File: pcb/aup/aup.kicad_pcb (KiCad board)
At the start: 6 copper layers, 50 x 50 mm, 7 parts, among them IC1 MT41K128M16JT-125_K, J1 DF40C-100DS-0.4V_51, J2 DF40C-100DS-0.4V_51, J3 DF40C-100DS-0.4V_51, J4 DF40C-100DS-0.4V_51, U1 XC7A50T-FGG484, U2 FT2232HL

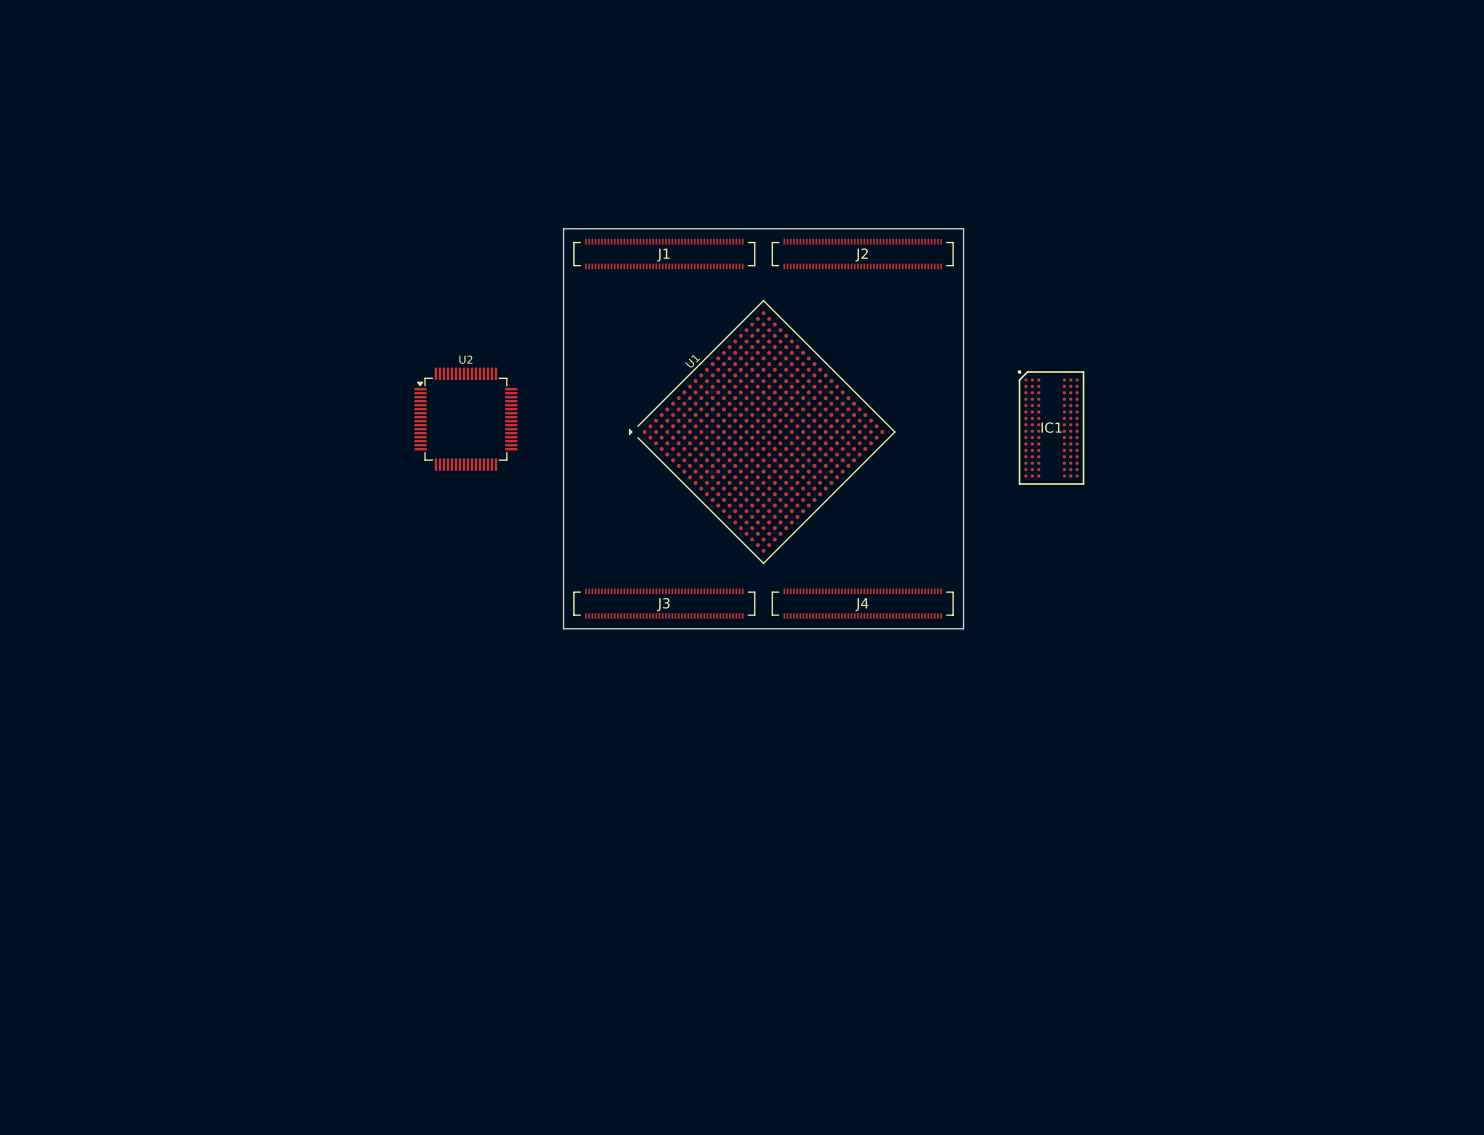
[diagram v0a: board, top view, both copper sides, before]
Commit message: Added symbols for the major components
It should be possible to do a first pass placement of ICs on the pcb as
a rough fit check.

Most imported footprints are still missing models.
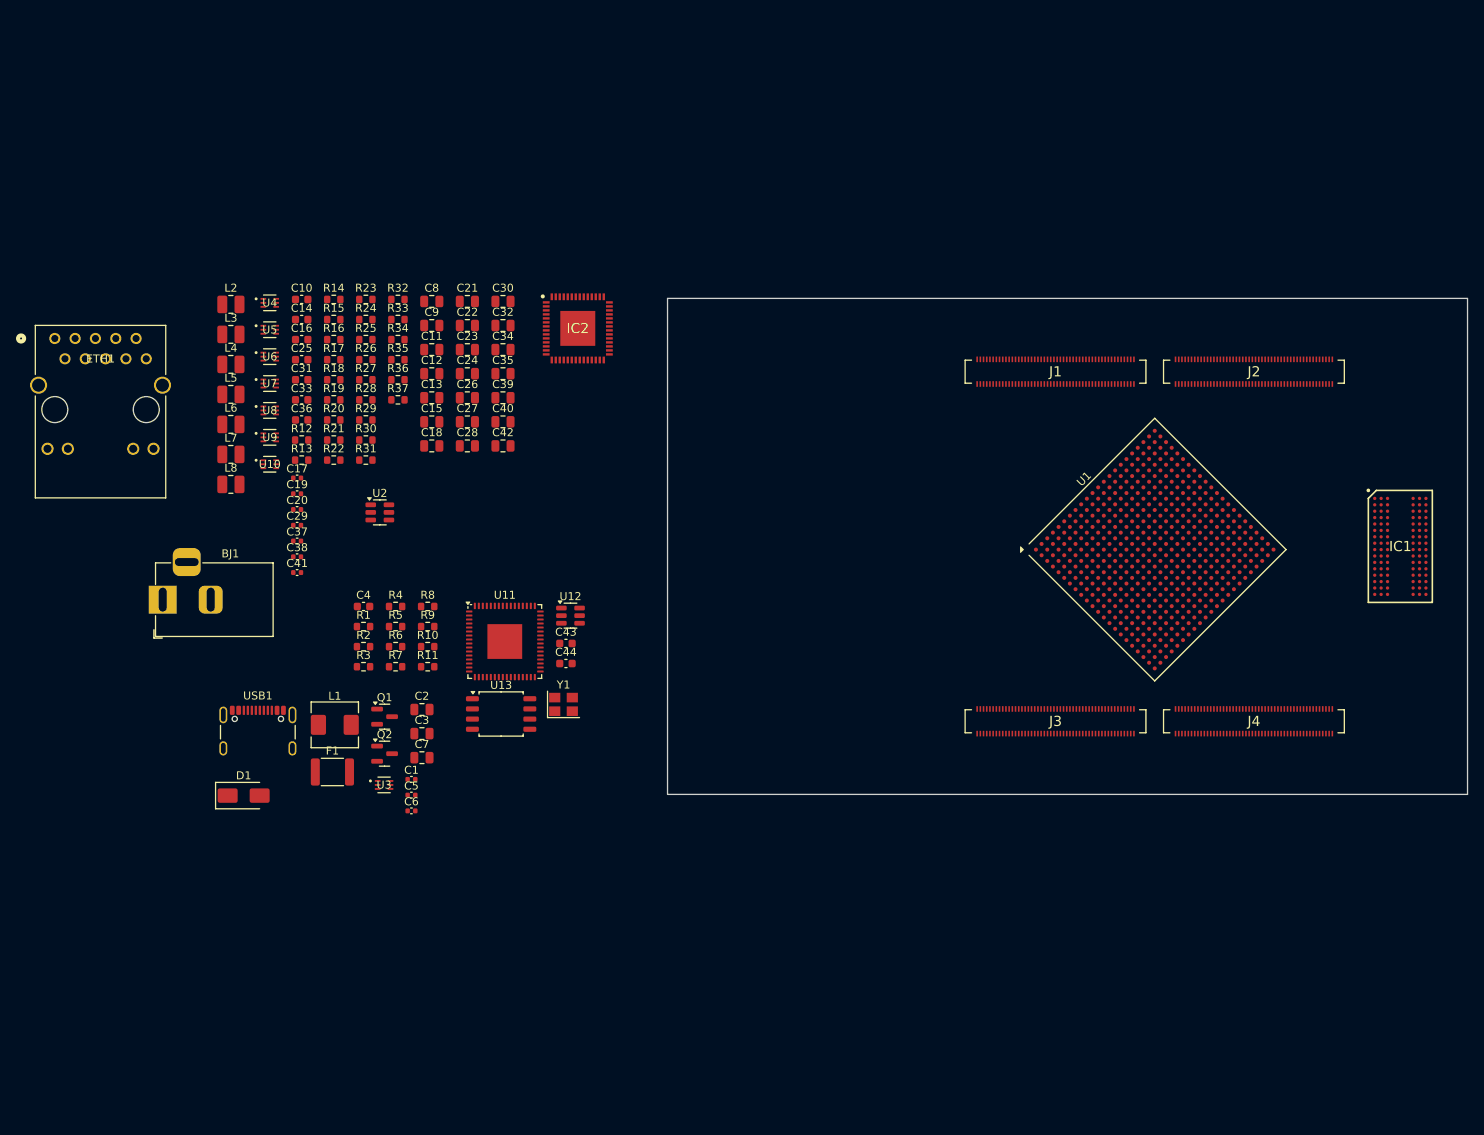
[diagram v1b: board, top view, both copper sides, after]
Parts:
- added BJ1: Barral_Jack_12V, Connector_BarrelJack:BarrelJack_Horizontal, F.Cu at (36.9, 87.4)
- added C1: 0.1uf, Capacitor_SMD:C_0402_1005Metric, F.Cu at (68.0, 109.8)
- added C10: 0.1uf/50v, Capacitor_SMD:C_0603_1608Metric, F.Cu at (54.3, 49.8)
- added C11: 10uf/50V, Capacitor_SMD:C_0805_2012Metric, F.Cu at (70.5, 56.1)
- added C12: 10uf/50V, Capacitor_SMD:C_0805_2012Metric, F.Cu at (70.5, 59.1)
- added C13: 10uf/50V, Capacitor_SMD:C_0805_2012Metric, F.Cu at (70.5, 62.1)
- added C14: 0.1uf/50v, Capacitor_SMD:C_0603_1608Metric, F.Cu at (54.3, 52.3)
- added C15: 10uf/50V, Capacitor_SMD:C_0805_2012Metric, F.Cu at (70.5, 65.1)
- added C16: 0.1uf/50v, Capacitor_SMD:C_0603_1608Metric, F.Cu at (54.3, 54.9)
- added C17: 0.1uf, Capacitor_SMD:C_0402_1005Metric, F.Cu at (53.7, 72.2)
- added C18: 22uf/25V, Capacitor_SMD:C_0805_2012Metric, F.Cu at (70.5, 68.1)
- added C19: 0.1uf, Capacitor_SMD:C_0402_1005Metric, F.Cu at (53.7, 74.1)
- added C2: 10uf/50V, Capacitor_SMD:C_0805_2012Metric, F.Cu at (69.3, 101.1)
- added C20: 0.1uf, Capacitor_SMD:C_0402_1005Metric, F.Cu at (53.7, 76.1)
- added C21: 10uf/50V, Capacitor_SMD:C_0805_2012Metric, F.Cu at (75.0, 50.1)
- added C22: 10uf/50V, Capacitor_SMD:C_0805_2012Metric, F.Cu at (75.0, 53.1)
- added C23: 22uf/25V, Capacitor_SMD:C_0805_2012Metric, F.Cu at (75.0, 56.1)
- added C24: 22uf/25V, Capacitor_SMD:C_0805_2012Metric, F.Cu at (75.0, 59.1)
- added C25: 0.1uf/50v, Capacitor_SMD:C_0603_1608Metric, F.Cu at (54.3, 57.4)
- added C26: 10uf/50V, Capacitor_SMD:C_0805_2012Metric, F.Cu at (75.0, 62.1)
- added C27: 10uf/50V, Capacitor_SMD:C_0805_2012Metric, F.Cu at (75.0, 65.1)
- added C28: 10uf/50V, Capacitor_SMD:C_0805_2012Metric, F.Cu at (75.0, 68.1)
- added C29: 0.1uf, Capacitor_SMD:C_0402_1005Metric, F.Cu at (53.7, 78.1)
- added C3: 10uf/50V, Capacitor_SMD:C_0805_2012Metric, F.Cu at (69.3, 104.1)
- added C30: 10uf/50V, Capacitor_SMD:C_0805_2012Metric, F.Cu at (79.4, 50.1)
- added C31: 0.1uf/50v, Capacitor_SMD:C_0603_1608Metric, F.Cu at (54.3, 59.9)
- added C32: 22uf/25V, Capacitor_SMD:C_0805_2012Metric, F.Cu at (79.4, 53.1)
- added C33: 0.1uf/50v, Capacitor_SMD:C_0603_1608Metric, F.Cu at (54.3, 62.4)
- added C34: 10uf/50V, Capacitor_SMD:C_0805_2012Metric, F.Cu at (79.4, 56.1)
- added C35: 10uf/50V, Capacitor_SMD:C_0805_2012Metric, F.Cu at (79.4, 59.1)
- added C36: 0.1uf/50v, Capacitor_SMD:C_0603_1608Metric, F.Cu at (54.3, 64.9)
- added C37: 0.1uf, Capacitor_SMD:C_0402_1005Metric, F.Cu at (53.7, 80.0)
- added C38: 0.1uf, Capacitor_SMD:C_0402_1005Metric, F.Cu at (53.7, 82.0)
- added C39: 22uf/25V, Capacitor_SMD:C_0805_2012Metric, F.Cu at (79.4, 62.1)
- added C4: 0.1uf/50v, Capacitor_SMD:C_0603_1608Metric, F.Cu at (62.0, 88.2)
- added C40: 22uf/25V, Capacitor_SMD:C_0805_2012Metric, F.Cu at (79.4, 65.1)
- added C41: 0.1uf, Capacitor_SMD:C_0402_1005Metric, F.Cu at (53.7, 84.0)
- added C42: 22uf/25V, Capacitor_SMD:C_0805_2012Metric, F.Cu at (79.4, 68.1)
- added C43: 30pf, Capacitor_SMD:C_0603_1608Metric, F.Cu at (87.3, 92.8)
- added C44: 30pf, Capacitor_SMD:C_0603_1608Metric, F.Cu at (87.3, 95.3)
- added C5: 33pf, Capacitor_SMD:C_0402_1005Metric, F.Cu at (68.0, 111.8)
- added C6: 0.1uf, Capacitor_SMD:C_0402_1005Metric, F.Cu at (68.0, 113.8)
- added C7: 22uf/25V, Capacitor_SMD:C_0805_2012Metric, F.Cu at (69.3, 107.1)
- added C8: 10uf/50V, Capacitor_SMD:C_0805_2012Metric, F.Cu at (70.5, 50.1)
- added C9: 10uf/50V, Capacitor_SMD:C_0805_2012Metric, F.Cu at (70.5, 53.1)
- added D1: SS34, Diode_SMD:D_SMA, F.Cu at (47.0, 111.8)
- added ETH1: HR911130A, !Misc:HR911130A_HAN, F.Cu at (23.4, 54.7)
- added F1: 2A, Fuse:Fuse_1812_4532Metric, F.Cu at (58.1, 108.9)
- added IC2: 88E1512-A0-NNP2C000, !Misc:QFN50P800X800X100-57N-D, F.Cu at (88.8, 53.5)
- added L1: 2.2uH/5A, Inductor_SMD:L_Sunlord_MWSA0518S, F.Cu at (58.4, 103.0)
- added L2: 1uH/2A, Inductor_SMD:L_1008_2520Metric, F.Cu at (45.4, 50.5)
- added L3: 1uH/2A, Inductor_SMD:L_1008_2520Metric, F.Cu at (45.4, 54.2)
- added L4: 2.2uH/2A, Inductor_SMD:L_1008_2520Metric, F.Cu at (45.4, 58.0)
- added L5: 1uH/2A, Inductor_SMD:L_1008_2520Metric, F.Cu at (45.4, 61.7)
- added L6: 2.2uH/2A, Inductor_SMD:L_1008_2520Metric, F.Cu at (45.4, 65.5)
- added L7: 2.2uH/2A, Inductor_SMD:L_1008_2520Metric, F.Cu at (45.4, 69.2)
- added L8: 1uH/2A, Inductor_SMD:L_1008_2520Metric, F.Cu at (45.4, 73.0)
- added Q1: AO3401A, Package_TO_SOT_SMD:SOT-23, F.Cu at (64.6, 102.0)
- added Q2: AO3401A, Package_TO_SOT_SMD:SOT-23, F.Cu at (64.6, 106.6)
- added R1: 10M, Resistor_SMD:R_0603_1608Metric, F.Cu at (62.0, 90.7)
- added R10: 20K, Resistor_SMD:R_0603_1608Metric, F.Cu at (70.0, 93.2)
- added R11: 100K, Resistor_SMD:R_0603_1608Metric, F.Cu at (70.0, 95.7)
- added R12: 10K, Resistor_SMD:R_0603_1608Metric, F.Cu at (54.3, 67.4)
- added R13: 150K, Resistor_SMD:R_0603_1608Metric, F.Cu at (54.3, 69.9)
- added R14: 51K, Resistor_SMD:R_0603_1608Metric, F.Cu at (58.3, 49.8)
- added R15: 51K, Resistor_SMD:R_0603_1608Metric, F.Cu at (58.3, 52.3)
- added R16: 51K, Resistor_SMD:R_0603_1608Metric, F.Cu at (58.3, 54.9)
- added R17: 10K, Resistor_SMD:R_0603_1608Metric, F.Cu at (58.3, 57.4)
- added R18: 10K, Resistor_SMD:R_0603_1608Metric, F.Cu at (58.3, 59.9)
- added R19: 10K, Resistor_SMD:R_0603_1608Metric, F.Cu at (58.3, 62.4)
- added R2: 5.1K, Resistor_SMD:R_0603_1608Metric, F.Cu at (62.0, 93.2)
- added R20: 15K, Resistor_SMD:R_0603_1608Metric, F.Cu at (58.3, 64.9)
- added R21: 43K, Resistor_SMD:R_0603_1608Metric, F.Cu at (58.3, 67.4)
- added R22: 4.99K, Resistor_SMD:R_0603_1608Metric, F.Cu at (58.3, 69.9)
- added R23: 15K, Resistor_SMD:R_0603_1608Metric, F.Cu at (62.3, 49.8)
- added R24: 10K, Resistor_SMD:R_0603_1608Metric, F.Cu at (62.3, 52.3)
- added R25: 20K, Resistor_SMD:R_0603_1608Metric, F.Cu at (62.3, 54.9)
- added R26: 4.99K, Resistor_SMD:R_0603_1608Metric, F.Cu at (62.3, 57.4)
- added R27: 20K, Resistor_SMD:R_0603_1608Metric, F.Cu at (62.3, 59.9)
- added R28: 10K, Resistor_SMD:R_0603_1608Metric, F.Cu at (62.3, 62.4)
- added R29: 10K, Resistor_SMD:R_0603_1608Metric, F.Cu at (62.3, 64.9)
- added R3: 5.1K, Resistor_SMD:R_0603_1608Metric, F.Cu at (62.0, 95.7)
- added R30: 20K, Resistor_SMD:R_0603_1608Metric, F.Cu at (62.3, 67.4)
- added R31: 10K, Resistor_SMD:R_0603_1608Metric, F.Cu at (62.3, 69.9)
- added R32: 15K, Resistor_SMD:R_0603_1608Metric, F.Cu at (66.3, 49.8)
- added R33: 30K, Resistor_SMD:R_0603_1608Metric, F.Cu at (66.3, 52.3)
- added R34: 10K, Resistor_SMD:R_0603_1608Metric, F.Cu at (66.3, 54.9)
- added R35: 10K, Resistor_SMD:R_0603_1608Metric, F.Cu at (66.3, 57.4)
- added R36: 20K, Resistor_SMD:R_0603_1608Metric, F.Cu at (66.3, 59.9)
- added R37: 10K, Resistor_SMD:R_0603_1608Metric, F.Cu at (66.3, 62.4)
- added R4: 10K, Resistor_SMD:R_0603_1608Metric, F.Cu at (66.0, 88.2)
- added R5: 100K, Resistor_SMD:R_0603_1608Metric, F.Cu at (66.0, 90.7)
- added R6: 20K, Resistor_SMD:R_0603_1608Metric, F.Cu at (66.0, 93.2)
- added R7: 10K, Resistor_SMD:R_0603_1608Metric, F.Cu at (66.0, 95.7)
- added R8: 150K, Resistor_SMD:R_0603_1608Metric, F.Cu at (70.0, 88.2)
- added R9: 10K, Resistor_SMD:R_0603_1608Metric, F.Cu at (70.0, 90.7)
- added U10: TPS563257DRLR, !Misc:SOT6_DRL_TEX, F.Cu at (50.3, 70.4)
- added U11: FT2232HQ, Package_DFN_QFN:QFN-64-1EP_9x9mm_P0.5mm_EP4.35x4.35mm, F.Cu at (79.7, 92.6)
- added U12: 93LC56BT-I/OT, Package_TO_SOT_SMD:SOT-23-6, F.Cu at (87.9, 89.4)
- added U13: MX25L3233FM2, Package_SO:SOIC-8_5.3x5.3mm_P1.27mm, F.Cu at (79.2, 101.7)
- added U3: TPS563257DRLR, !Misc:SOT6_DRL_TEX, F.Cu at (64.6, 110.5)
- added U4: TPS563257DRLR, !Misc:SOT6_DRL_TEX, F.Cu at (50.3, 50.3)
- added U5: TPS563257DRLR, !Misc:SOT6_DRL_TEX, F.Cu at (50.3, 53.6)
- added U6: TPS563257DRLR, !Misc:SOT6_DRL_TEX, F.Cu at (50.3, 57.0)
- added U7: TPS563257DRLR, !Misc:SOT6_DRL_TEX, F.Cu at (50.3, 60.3)
- added U8: TPS563257DRLR, !Misc:SOT6_DRL_TEX, F.Cu at (50.3, 63.7)
- added U9: TPS563257DRLR, !Misc:SOT6_DRL_TEX, F.Cu at (50.3, 67.1)
- added USB1: USB_C_Receptacle_USB2.0_16P, !Misc:USB_C_Receptacle_GCT_USB4105-xx-A_16P_TopMnt_Horizontal, F.Cu at (48.8, 104.9)
- added Y1: 12MHz/20pf, Crystal:Crystal_SMD_3225-4Pin_3.2x2.5mm, F.Cu at (87.0, 100.5)
- U2: value FT2232HL -> USBLC6-2SC6; footprint Package_QFP:LQFP-64_10x10mm_P0.5mm -> Package_TO_SOT_SMD:SOT-23-6
- moved J1 51.1 mm to (148.5, 58.9)
- moved J2 51.1 mm to (173.3, 58.9)
- moved J3 51.1 mm to (148.5, 102.6)
- moved J4 51.1 mm to (173.3, 102.6)
- moved U1 51.1 mm to (160.9, 81.1)
- moved IC1 46.0 mm to (191.6, 80.7)
- moved U2 15.9 mm to (64.0, 76.5)
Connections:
- U1 pad A11: GND -> unconnected-(U1G-GND-PadA11)
- U1 pad A12: GND -> unconnected-(U1G-GND-PadA12)
- U1 pad A2: GND -> unconnected-(U1G-GND-PadA2)
- U1 pad A22: GND -> unconnected-(U1G-GND-PadA22)
- U1 pad A3: GND -> unconnected-(U1G-GND-PadA3)
- U1 pad A5: GND -> unconnected-(U1G-GND-PadA5)
- U1 pad A7: GND -> unconnected-(U1G-GND-PadA7)
- U1 pad A9: GND -> unconnected-(U1G-GND-PadA9)
- U1 pad AA12: GND -> unconnected-(U1G-GND-PadAA12)
- U1 pad AA2: GND -> unconnected-(U1G-GND-PadAA2)
- U1 pad AA22: GND -> unconnected-(U1G-GND-PadAA22)
- U1 pad AB19: GND -> unconnected-(U1G-GND-PadAB19)
- U1 pad AB9: GND -> unconnected-(U1G-GND-PadAB9)
- U1 pad B12: GND -> unconnected-(U1G-GND-PadB12)
- U1 pad B19: GND -> unconnected-(U1G-GND-PadB19)
- U1 pad B3: GND -> unconnected-(U1G-GND-PadB3)
- U1 pad C10: GND -> unconnected-(U1G-GND-PadC10)
- U1 pad C12: GND -> unconnected-(U1G-GND-PadC12)
- U1 pad C16: GND -> unconnected-(U1G-GND-PadC16)
- U1 pad C3: GND -> unconnected-(U1G-GND-PadC3)
- U1 pad C6: GND -> unconnected-(U1G-GND-PadC6)
- U1 pad D12: GND -> unconnected-(U1G-GND-PadD12)
- U1 pad D13: GND -> unconnected-(U1G-GND-PadD13)
- U1 pad D3: GND -> unconnected-(U1G-GND-PadD3)
- U1 pad D4: GND -> unconnected-(U1G-GND-PadD4)
- U1 pad D8: GND -> unconnected-(U1G-GND-PadD8)
- U1 pad E11: GND -> unconnected-(U1G-GND-PadE11)
- U1 pad E20: GND -> unconnected-(U1G-GND-PadE20)
- U1 pad E4: GND -> unconnected-(U1G-GND-PadE4)
- U1 pad E5: GND -> unconnected-(U1G-GND-PadE5)
- U1 pad E7: GND -> unconnected-(U1G-GND-PadE7)
- U1 pad E9: GND -> unconnected-(U1G-GND-PadE9)
- U1 pad F11: GND -> unconnected-(U1G-GND-PadF11)
- U1 pad F17: GND -> unconnected-(U1G-GND-PadF17)
- U1 pad F5: GND -> unconnected-(U1G-GND-PadF5)
- U1 pad G10: GND -> unconnected-(U1G-GND-PadG10)
- U1 pad G12: GND -> unconnected-(U1G-GND-PadG12)
- U1 pad G14: GND -> unconnected-(U1G-GND-PadG14)
- U1 pad G5: GND -> unconnected-(U1G-GND-PadG5)
- U1 pad G6: GND -> unconnected-(U1G-GND-PadG6)
- U1 pad G7: GND -> unconnected-(U1G-GND-PadG7)
- U1 pad G8: GND -> unconnected-(U1G-GND-PadG8)
- U1 pad G9: GND -> unconnected-(U1G-GND-PadG9)
- U1 pad H1: GND -> unconnected-(U1G-GND-PadH1)
- U1 pad H11: GND -> unconnected-(U1G-GND-PadH11)
- U1 pad H21: GND -> unconnected-(U1G-GND-PadH21)
- U1 pad H7: GND -> unconnected-(U1G-GND-PadH7)
- U1 pad H9: GND -> unconnected-(U1G-GND-PadH9)
- U1 pad J10: GND -> unconnected-(U1G-GND-PadJ10)
- U1 pad J12: GND -> unconnected-(U1G-GND-PadJ12)
- U1 pad J18: GND -> unconnected-(U1G-GND-PadJ18)
- U1 pad J8: GND -> unconnected-(U1G-GND-PadJ8)
- U1 pad K11: GND -> unconnected-(U1G-GND-PadK11)
- U1 pad K15: GND -> unconnected-(U1G-GND-PadK15)
- U1 pad K5: GND -> unconnected-(U1G-GND-PadK5)
- U1 pad K7: GND -> unconnected-(U1G-GND-PadK7)
- U1 pad L2: GND -> unconnected-(U1G-GND-PadL2)
- U1 pad L22: GND -> unconnected-(U1G-GND-PadL22)
- U1 pad L8: GND -> unconnected-(U1G-GND-PadL8)
- U1 pad M11: GND -> unconnected-(U1G-GND-PadM11)
- U1 pad M19: GND -> unconnected-(U1G-GND-PadM19)
- U1 pad M7: GND -> unconnected-(U1G-GND-PadM7)
- U1 pad N16: GND -> unconnected-(U1G-GND-PadN16)
- U1 pad N6: GND -> unconnected-(U1G-GND-PadN6)
- U1 pad N8: GND -> unconnected-(U1G-GND-PadN8)
- U1 pad P11: GND -> unconnected-(U1G-GND-PadP11)
- U1 pad P13: GND -> unconnected-(U1G-GND-PadP13)
- U1 pad P3: GND -> unconnected-(U1G-GND-PadP3)
- U1 pad P7: GND -> unconnected-(U1G-GND-PadP7)
- U1 pad P9: GND -> unconnected-(U1G-GND-PadP9)
- U1 pad R10: GND -> unconnected-(U1G-GND-PadR10)
- U1 pad R12: GND -> unconnected-(U1G-GND-PadR12)
- U1 pad R20: GND -> unconnected-(U1G-GND-PadR20)
- U1 pad R8: GND -> unconnected-(U1G-GND-PadR8)
- U1 pad T11: GND -> unconnected-(U1G-GND-PadT11)
- U1 pad T17: GND -> unconnected-(U1G-GND-PadT17)
- U1 pad T7: GND -> unconnected-(U1G-GND-PadT7)
- U1 pad T9: GND -> unconnected-(U1G-GND-PadT9)
- U1 pad U14: GND -> unconnected-(U1G-GND-PadU14)
- U1 pad U4: GND -> unconnected-(U1G-GND-PadU4)
- U1 pad V1: GND -> unconnected-(U1G-GND-PadV1)
- U1 pad V11: GND -> unconnected-(U1G-GND-PadV11)
- U1 pad V21: GND -> unconnected-(U1G-GND-PadV21)
- U1 pad W18: GND -> unconnected-(U1G-GND-PadW18)
- U1 pad W8: GND -> unconnected-(U1G-GND-PadW8)
- U1 pad Y15: GND -> unconnected-(U1G-GND-PadY15)
- U1 pad Y5: GND -> unconnected-(U1G-GND-PadY5)
- U2 pad 1: unconnected-(U2-GND-Pad1) -> /ext_power/USB_DN
- U2 pad 2: unconnected-(U2-OSCI-Pad2) -> GND
- U2 pad 3: unconnected-(U2-OSCO-Pad3) -> /ext_power/USB_DP
- U2 pad 4: unconnected-(U2-VPHY-Pad4) -> DP
- U2 pad 5: unconnected-(U2-GND-Pad5) -> /ext_power/5V_USB
- U2 pad 6: unconnected-(U2-REF-Pad6) -> DN
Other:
- board size 50 x 50 mm -> 100 x 62 mm

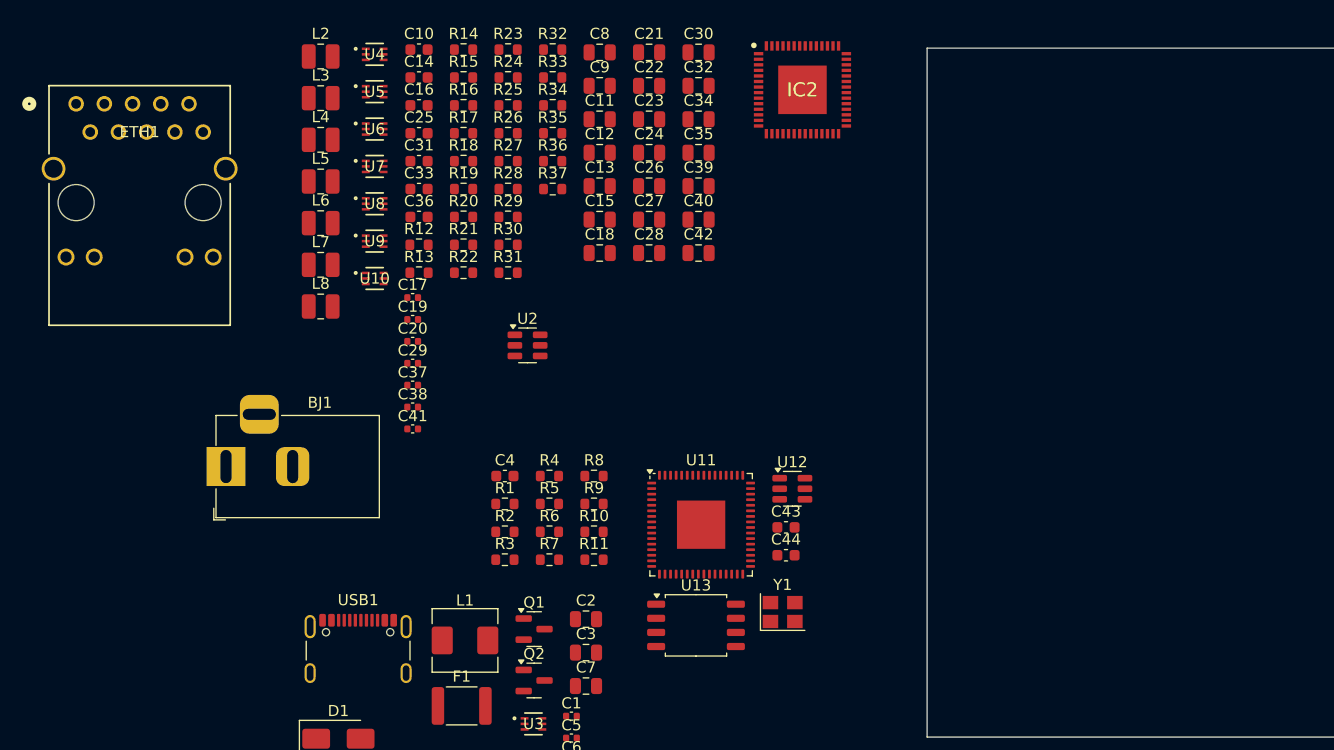
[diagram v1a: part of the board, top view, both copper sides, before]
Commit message: Initial layout for Vccint
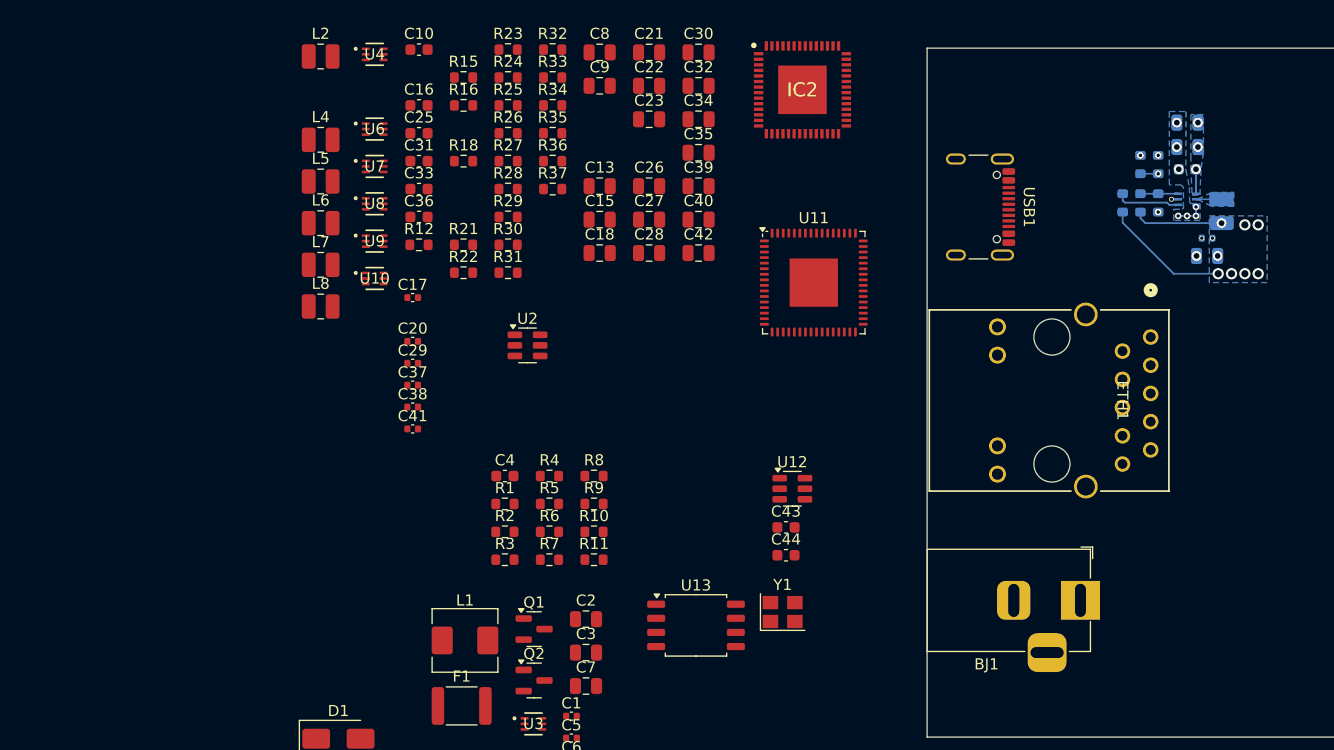
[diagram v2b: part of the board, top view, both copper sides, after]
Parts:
- C11, C12, C14, C19, C24, L3, R13, R14, R17, R19, R20, U5: moved to B.Cu
- moved ETH1 99.0 mm to (120.1, 75.7), turned to -90 degrees
- moved L3 81.7 mm to (126.5, 64.4), turned to -90 degrees
- moved BJ1 77.8 mm to (113.8, 99.4), turned to 0 degrees
- moved U5 73.8 mm to (123.4, 63.3), turned to 180 degrees
- moved C19 71.9 mm to (125.2, 66.8), turned to 180 degrees
- moved C14 69.6 mm to (123.4, 60.6), turned to 180 degrees
- moved USB1 68.4 mm to (103.7, 64.0), turned to -90 degrees
- moved R13 65.7 mm to (119.2, 60.2), turned to -90 degrees
- moved R14 63.4 mm to (120.8, 60.2), turned to 90 degrees
- moved R20 62.5 mm to (120.8, 63.6), turned to -90 degrees
- moved R19 60.9 mm to (119.2, 63.6), turned to 90 degrees
- moved R17 59.6 mm to (117.6, 63.6), turned to -90 degrees
- moved C12 53.0 mm to (123.4, 56.4), turned to 180 degrees
- moved C11 53.0 mm to (123.4, 58.6), turned to 180 degrees
- moved C24 51.1 mm to (125.2, 68.4), turned to 180 degrees
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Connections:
- net Net-(U5-EN) renamed /power_reg/EN_Vccint
- net Net-(U5-FB) renamed /power_reg/FB_Vccint
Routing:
- net +Vccint: track 0.00 -> 19.5 mm, vias 0 -> 9
- net /power_reg/PG_Vccint: track 0.00 -> 5.77 mm
- net /power_reg/FB_Vccint: track 0.00 -> 3.41 mm
- net GND: track 0.00 -> 2.60 mm, vias 0 -> 11
- net /power_reg/SW_Vccint: track 0.00 -> 2.30 mm
- net /power_reg/EN_Vccint: track 0.00 -> 2.24 mm, vias 0 -> 2
- net +5V: track 0.00 -> 2.20 mm, vias 0 -> 4
- added copper zone on B.Cu, net +5V
- added copper zone on B.Cu, net +Vccint
- added copper zone on B.Cu, net /power_reg/SW_Vccint
- added copper zone on B.Cu, net GND

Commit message: Rough high level layout plan
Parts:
- moved U13 73.2 mm to (119.8, 40.7)
- moved C24 64.9 mm to (74.9, 27.4)
- moved C11 64.9 mm to (73.1, 17.6)
- moved C12 64.9 mm to (73.1, 15.4)
- moved C14 64.9 mm to (73.1, 19.6)
- moved C19 64.9 mm to (74.9, 25.8)
- moved R13 64.9 mm to (68.9, 19.2)
- moved R14 64.9 mm to (70.5, 19.2)
- moved R17 64.9 mm to (67.3, 22.6)
- moved R19 64.9 mm to (68.9, 22.6)
- moved R20 64.9 mm to (70.5, 22.6)
- moved U5 64.9 mm to (73.1, 22.3)
- moved L3 64.9 mm to (76.2, 23.4)
- moved U12 54.4 mm to (111.4, 40.2)
- moved R5 53.0 mm to (79.0, 142.1)
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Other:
- board size 100 x 62 mm -> 100 x 100 mm
